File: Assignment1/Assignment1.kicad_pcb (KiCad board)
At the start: 2 copper layers, 50 x 50 mm, 22 parts, among them J1 Conn_01x02_Pin, J2 Conn_01x02_Pin, U1 TPS51386RJNR

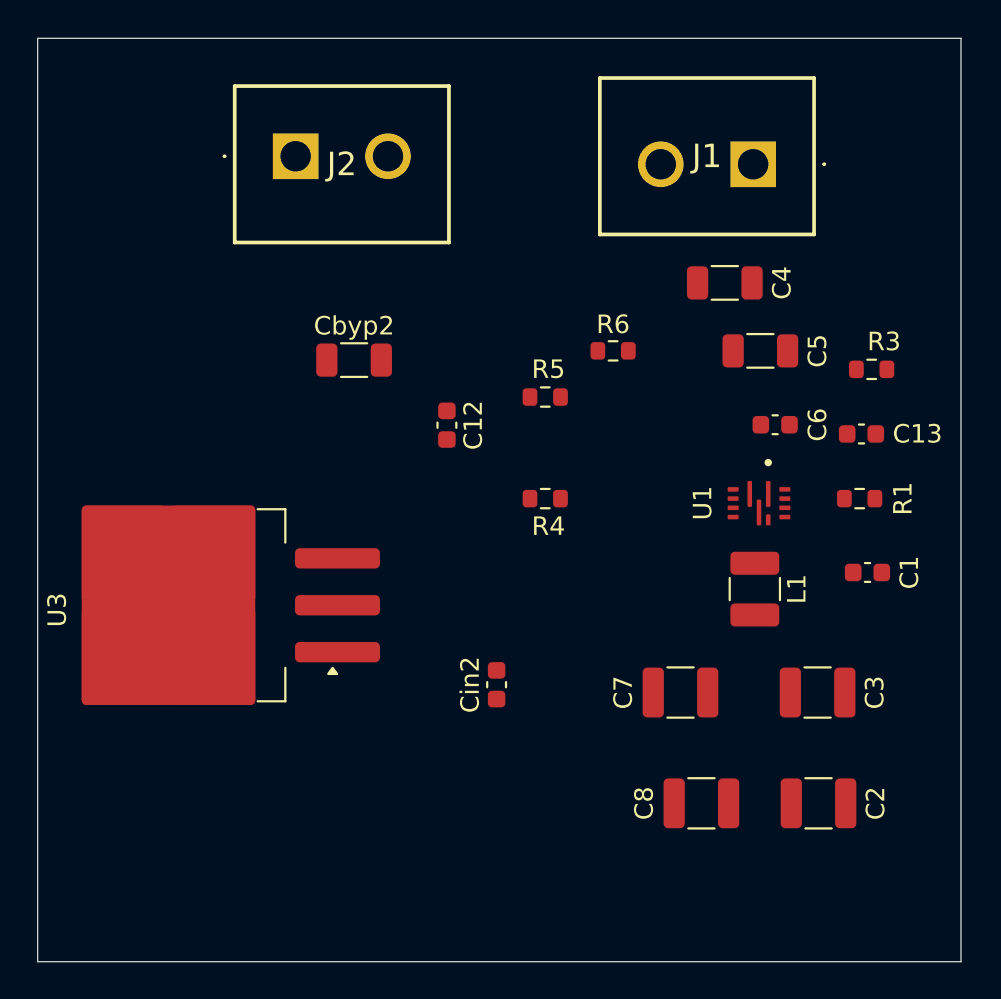
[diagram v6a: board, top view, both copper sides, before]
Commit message: assignment1: route pcb
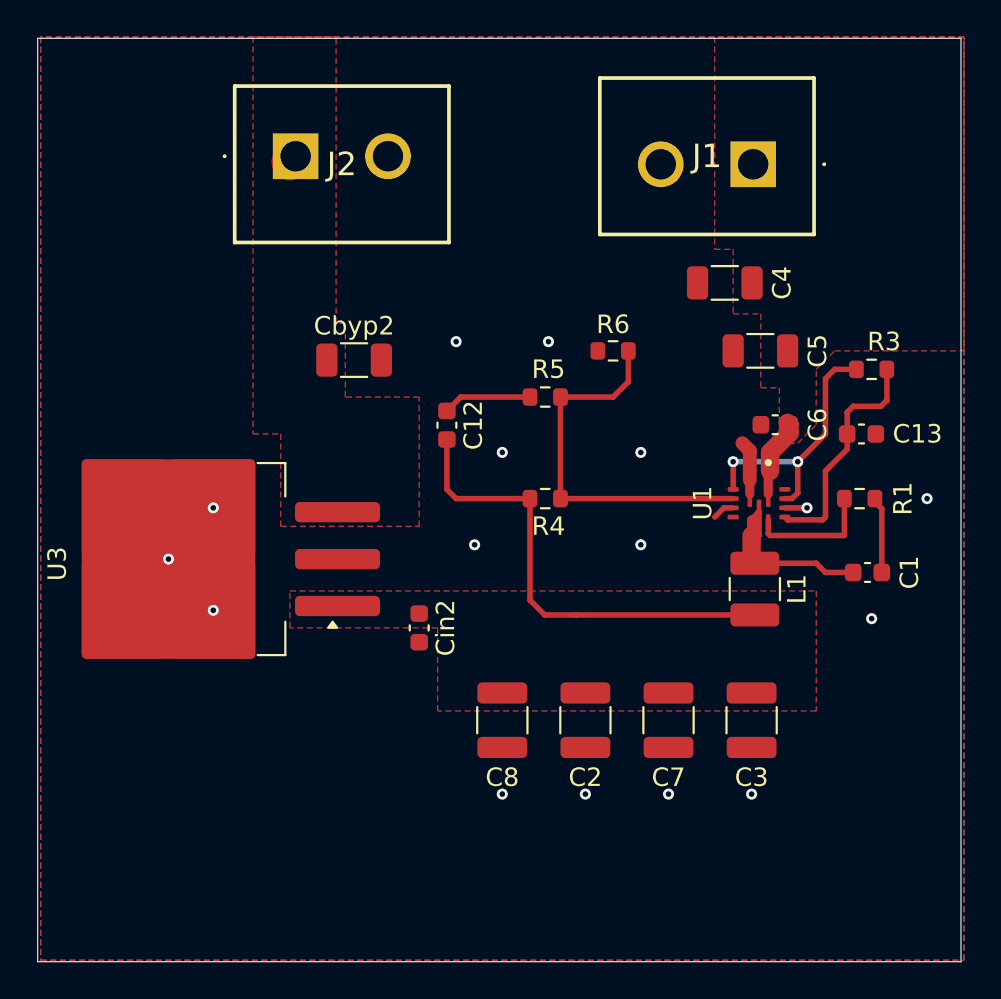
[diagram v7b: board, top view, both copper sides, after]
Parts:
- C1, C6: value 0.1uF -> 0.1μF
- C13, Cin2: value 1uF -> 1μF
- C2, C3, C7, C8: value 22uF -> 22μF
- C4, C5: value 10uF -> 10μF
- Cbyp2: value 47uF -> 47μF
- L1: value 1.5uH -> 1.5μH
- moved C2 13.4 mm to (80.5, 87.0), turned to -90 degrees
- moved C8 11.7 mm to (76.0, 87.0), turned to -90 degrees
- moved Cin2 5.20 mm to (71.5, 82.0), turned to -90 degrees
- moved C3 3.88 mm to (89.5, 87.0), turned to -90 degrees
- moved U3 2.50 mm to (59.4, 78.3)
- moved C7 1.63 mm to (85.0, 87.0), turned to -90 degrees
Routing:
- net /BuckStep_Vout: track 0.00 -> 25.4 mm
- net /Buck_FB: track 0.00 -> 20.5 mm
- net /Buck_PG: track 0.00 -> 14.5 mm, vias 0 -> 2
- net /Buck_Vcc: track 0.00 -> 12.6 mm
- net /Buck_SW: track 0.00 -> 9.68 mm
- net /Buck_VBST: track 0.00 -> 6.90 mm
- net Earth: track 0.00 -> 5.32 mm, vias 0 -> 16
- net Net-(C12-Pad1): track 0.00 -> 4.81 mm
- net /Buck_Vin: track 0.00 -> 4.58 mm
- net Net-(C1-Pad1): track 0.00 -> 4.16 mm
- added copper zone on F.Cu, net /BuckStep_Vout
- added copper zone on F.Cu, net /Buck_Vin
- added copper zone on F.Cu, net /Vout
- added copper zone on B.Cu, net Earth
- added copper zone on F.Cu, net Earth

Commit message: as1: reroute stuff
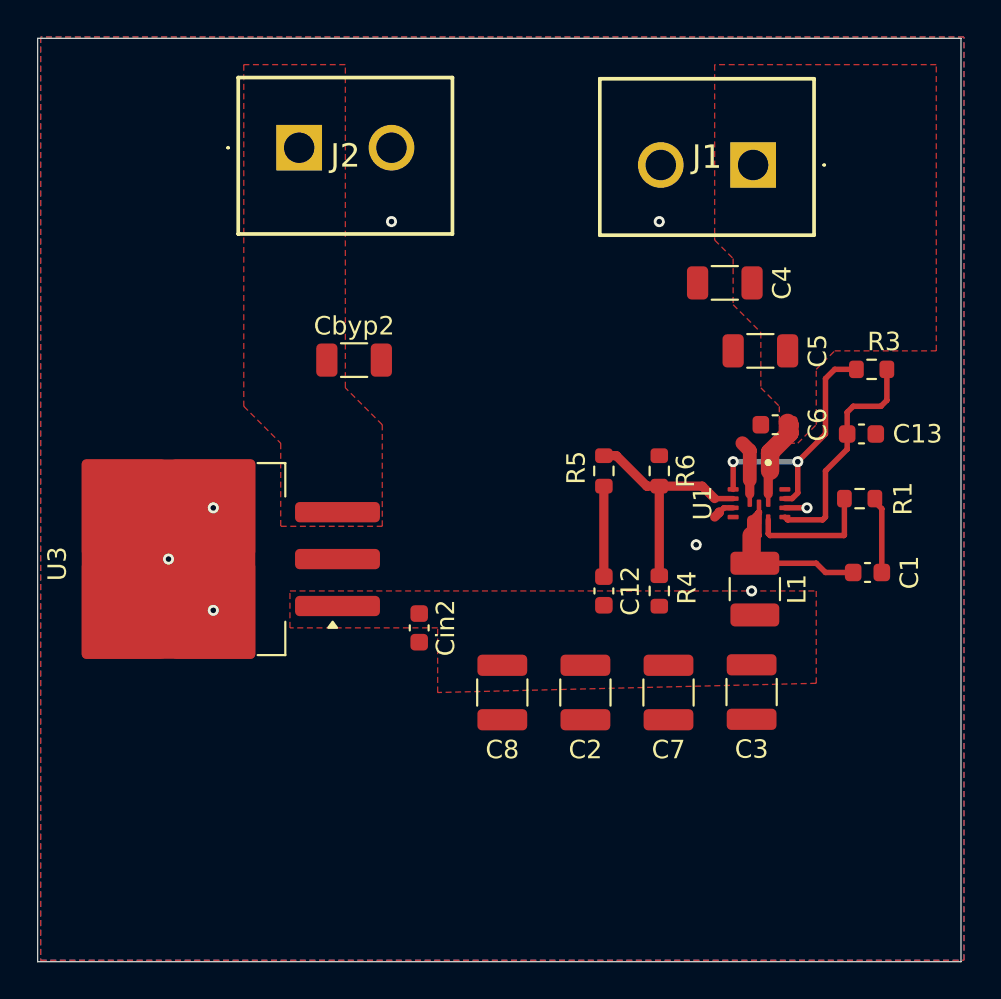
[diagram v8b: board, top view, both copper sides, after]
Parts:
- moved C12 12.4 mm to (81.5, 80.0)
- moved R4 7.95 mm to (84.5, 80.0), turned to -90 degrees
- moved R6 6.96 mm to (84.5, 73.5), turned to -90 degrees
- moved R5 5.11 mm to (81.5, 73.5), turned to -90 degrees
- moved C3 1.53 mm to (89.5, 85.5)
- moved C2 1.50 mm to (80.5, 85.5)
- moved C7 1.50 mm to (85.0, 85.5)
- moved C8 1.50 mm to (76.0, 85.5)
- moved J2 0.50 mm to (65.0, 56.0)
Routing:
- net /BuckStep_Vout: track 25.4 -> 0.00 mm
- net /Buck_FB: track 20.5 -> 12.8 mm
- net Earth: track 5.32 -> 5.71 mm, vias 16 -> 8
